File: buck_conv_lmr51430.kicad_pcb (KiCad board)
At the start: 2 copper layers, 43.2 x 17.4 mm, 10 parts, among them J1 Screw_Terminal_01x02, J2 Screw_Terminal_01x02

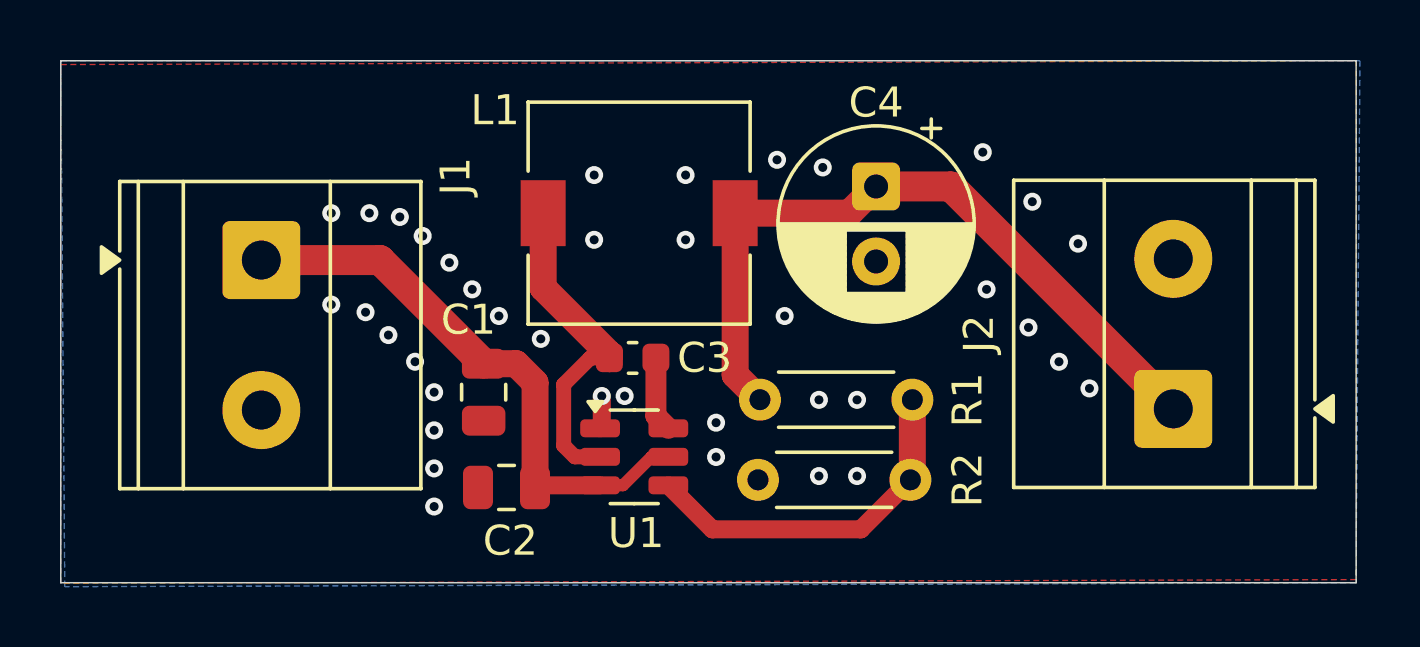
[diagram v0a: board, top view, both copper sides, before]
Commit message: Add variable output feedback network
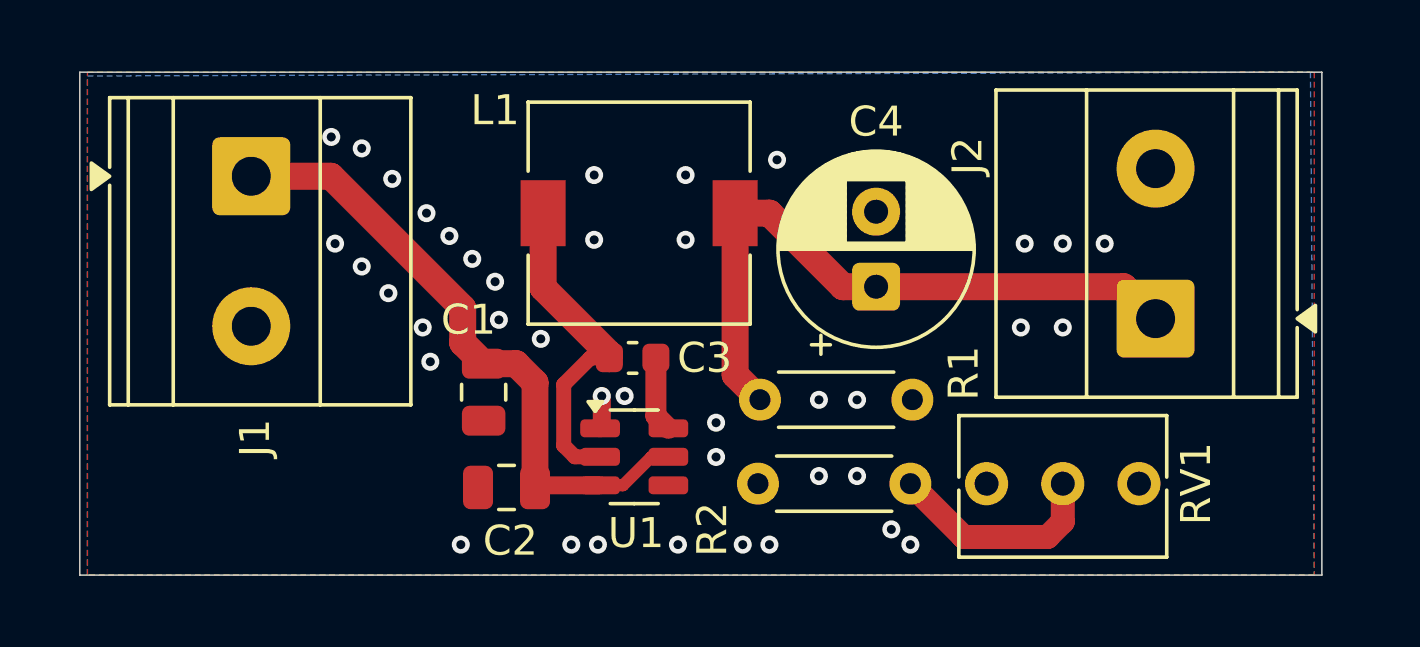
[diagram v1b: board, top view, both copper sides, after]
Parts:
- added RV1: 200k, Potentiometer_THT:Potentiometer_Bourns_3266Y_Vertical, F.Cu at (137.5, 96.6)
- moved R2 5.08 mm to (124.8, 96.6), turned to 0 degrees
- moved C4 3.34 mm to (128.8, 90.1), turned to 90 degrees
- moved J2 3.07 mm to (138.1, 91.1)
- moved J1 2.81 mm to (108.0, 86.4)
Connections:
- R1 pad 2: Net-(U1-FB) -> GND
- R2 pad 1: Net-(U1-FB) -> GND
- R2 pad 2: GND -> Net-(R2-Pad2)
- U1 pad 4: Net-(U1-FB) -> GND
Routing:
- net Net-(U1-FB): track 12.4 -> 0.00 mm
- net Net-(R2-Pad2): track 0.00 -> 7.39 mm
- net Net-(J2-Pin_1): track 24.6 -> 22.1 mm
- net Net-(J1-Pin_1): track 19.5 -> 21.7 mm
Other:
- board size 43.2 x 17.4 mm -> 41.4 x 16.8 mm

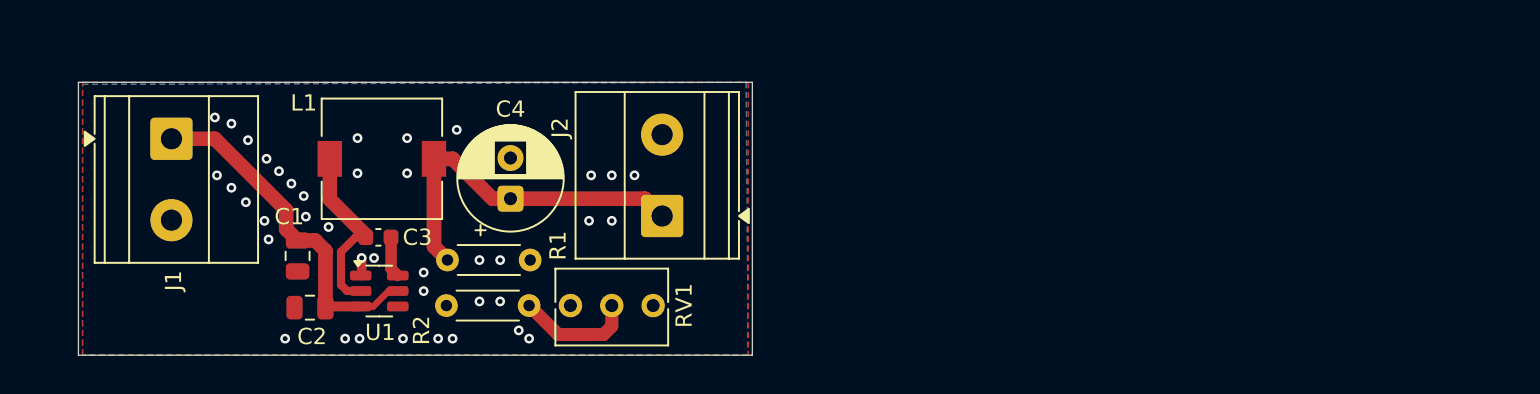
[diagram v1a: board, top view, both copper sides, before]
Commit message: Inductor selection and footprint fix
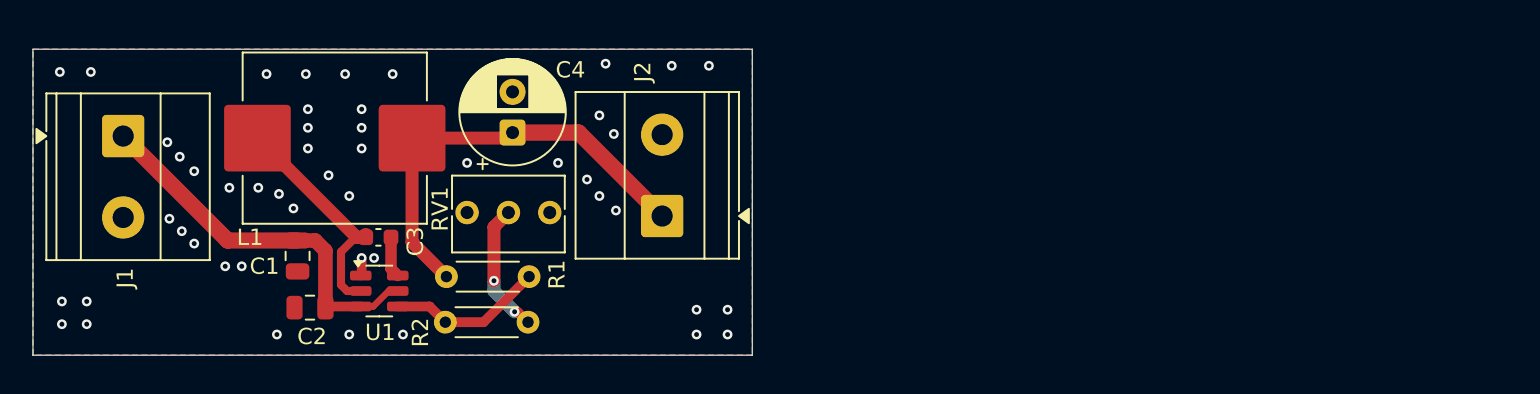
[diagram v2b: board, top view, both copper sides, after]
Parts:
- L1: footprint Inductor_SMD:L_7.3x7.3_H4.5 -> Inductor_SMD:L_APV_APH1030
- moved RV1 8.54 mm to (131.2, 90.9)
- moved C4 4.07 mm to (128.9, 86.0)
- moved L1 3.16 mm to (118.0, 86.4)
- moved J1 2.97 mm to (105.0, 86.2)
- moved R1 1.02 mm to (124.8, 94.9)
- moved R2 1.02 mm to (124.8, 97.7)
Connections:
- R1 pad 2: GND -> Net-(U1-FB)
- R2 pad 1: GND -> Net-(U1-FB)
- U1 pad 4: GND -> Net-(U1-FB)
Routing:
- net Net-(U1-FB): track 0.00 -> 9.98 mm
- net Net-(J2-Pin_1): track 22.1 -> 27.0 mm
- net Net-(U1-SW): track 11.4 -> 15.0 mm
- net Net-(J1-Pin_1): track 21.7 -> 24.0 mm
- net Net-(R2-Pad2): track 7.39 -> 8.08 mm, vias 0 -> 2
- net GND: track 1.45 -> 1.10 mm, vias 40 -> 49
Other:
- board size 41.4 x 16.8 mm -> 44.2 x 18.8 mm

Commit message: changes regarding the inductor
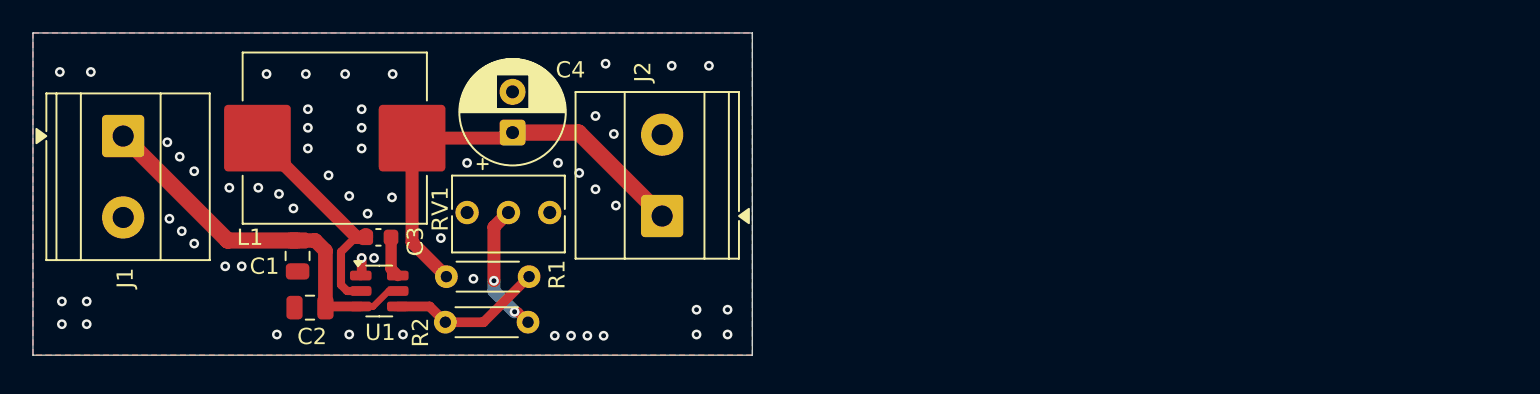
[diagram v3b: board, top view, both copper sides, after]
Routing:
- net GND: vias 49 -> 57
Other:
- board size 44.2 x 18.8 mm -> 44.2 x 19.8 mm
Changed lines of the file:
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@@
 			)
 		)
-		(property "Datasheet" ""
+		(property "Datasheet" "~"
 			(at 0 0 90)
 			(layer "F.Fab")
@@
 			)
 		)
-		(property "Datasheet" ""
+		(property "Datasheet" "~"
 			(at 0 0 90)
 			(layer "F.Fab")
@@
 			)
 		)
-		(property "Datasheet" ""
+		(property "Datasheet" "~"
 			(at 0 0 0)
 			(layer "F.Fab")
@@
 			)
 		)
-		(property "Datasheet" ""
+		(property "Datasheet" "~"
 			(at 0 0 0)
 			(layer "F.Fab")
@@
 			)
 		)
-		(property "Datasheet" ""
+		(property "Datasheet" "~"
 			(at 0 0 0)
 			(layer "F.Fab")
@@
 			)
 		)
-		(property "Datasheet" ""
+		(property "Datasheet" "~"
 			(at 0 0 90)
 			(layer "F.Fab")
@@
 			)
 		)
-		(property "Datasheet" ""
+		(property "Datasheet" "~"
 			(at 0 0 90)
 			(layer "F.Fab")
@@
 			)
 		)
-		(property "Datasheet" ""
+		(property "Datasheet" "~"
 			(at 0 0 0)
 			(layer "F.Fab")
@@
 			)
 		)
-		(property "Datasheet" ""
+		(property "Datasheet" "~"
 			(at 0 0 0)
 			(layer "F.Fab")
@@
 			)
 		)
-		(property "Datasheet" ""
+		(property "Datasheet" "~"
 			(at 0 0 0)
 			(layer "F.Fab")
@@
 	)
 	(gr_rect
-		(start 99.441 80.899)
+		(start 99.441 79.899)
 		(end 143.637 99.695)
 		(stroke
@@
 	)
 	(via
+		(at 120 91)
+		(size 0.6)
+		(drill 0.3)
+		(layers "F.Cu" "B.Cu")
+		(free yes)
+		(net 1)
+	)
+	(via
 		(at 112.268 94.234)
 		(size 0.6)
@@
 	)
 	(via
-		(at 134.239 84.963)
+		(at 134 85)
 		(size 0.6)
 		(drill 0.3)
@@
 	)
 	(via
+		(at 132.5 98.5)
+		(size 0.6)
+		(drill 0.3)
+		(layers "F.Cu" "B.Cu")
+		(free yes)
+		(net 1)
+	)
+	(via
 		(at 111.506 89.408)
 		(size 0.6)
@@
 	)
 	(via
-		(at 133.477 88.9)
+		(at 126.5 95)
+		(size 0.6)
+		(drill 0.3)
+		(layers "F.Cu" "B.Cu")
+		(free yes)
+		(net 1)
+	)
+	(via
+		(at 133 88.5)
 		(size 0.6)
 		(drill 0.3)
@@
 	)
 	(via
+		(at 134.5 98.5)
+		(size 0.6)
+		(drill 0.3)
+		(layers "F.Cu" "B.Cu")
+		(free yes)
+		(net 1)
+	)
+	(via
 		(at 113.284 89.408)
 		(size 0.6)
@@
 	)
 	(via
+		(at 133.5 98.5)
+		(size 0.6)
+		(drill 0.3)
+		(layers "F.Cu" "B.Cu")
+		(free yes)
+		(net 1)
+	)
+	(via
 		(at 116.205 82.423)
 		(size 0.6)
@@
 	)
 	(via
-		(at 135.255 90.805)
+		(at 135.255 90.5)
 		(size 0.6)
 		(drill 0.3)
@@
 	)
 	(via
-		(at 134.239 89.916)
+		(at 131.5 98.5)
+		(size 0.6)
+		(drill 0.3)
+		(layers "F.Cu" "B.Cu")
+		(free yes)
+		(net 1)
+	)
+	(via
+		(at 134 89.5)
 		(size 0.6)
 		(drill 0.3)
@@
 	)
 	(via
+		(at 124.5 92.5)
+		(size 0.6)
+		(drill 0.3)
+		(layers "F.Cu" "B.Cu")
+		(free yes)
+		(net 1)
+	)
+	(via
+		(at 121.5 90)
+		(size 0.6)
+		(drill 0.3)
+		(layers "F.Cu" "B.Cu")
+		(free yes)
+		(net 1)
+	)
+	(via
 		(at 116.332 86.995)
 		(size 0.6)
@@
 	)
 	(segment
-		(start 119.888 92.837)
-		(end 119.888 92.456)
-		(width 0.2)
-		(layer "F.Cu")
-		(net 3)
-	)
-	(segment
 		(start 118.364 95.377)
 		(end 118.364 93.345)
@@
 		(polygon
 			(pts
-				(xy 99.441 80.899) (xy 143.637 80.899) (xy 143.637 99.695) (xy 99.441 99.695)
+				(xy 99.441 79.899) (xy 143.637 79.899) (xy 143.637 99.695) (xy 99.441 99.695)
 			)
 		)
@@
 		(polygon
 			(pts
-				(xy 99.441 80.899) (xy 143.637 80.899) (xy 143.637 99.695) (xy 99.441 99.695)
+				(xy 99.441 79.899) (xy 143.637 79.899) (xy 143.637 99.695) (xy 99.441 99.695)
 			)
 		)

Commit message: rajath final touches
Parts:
- added C5: 22u, Capacitor_SMD:C_0805_2012Metric_Pad1.18x1.45mm_HandSolder, F.Cu at (169.0, 90.0)
- added C6: 22u, Capacitor_SMD:C_0805_2012Metric_Pad1.18x1.45mm_HandSolder, F.Cu at (175.0, 90.0)
- C1: value 1uF -> 4.7u; footprint Capacitor_SMD:C_0805_2012Metric -> Capacitor_SMD:C_0805_2012Metric_Pad1.18x1.45mm_HandSolder
- C2: value 100nF -> 100n; footprint Capacitor_SMD:C_0805_2012Metric -> Capacitor_SMD:C_0805_2012Metric_Pad1.18x1.45mm_HandSolder
- C3: value 100nF -> 100n; footprint Capacitor_SMD:C_0603_1608Metric -> Capacitor_SMD:C_0805_2012Metric_Pad1.18x1.45mm_HandSolder
- C4: value 100uF -> 22u; footprint Capacitor_THT:CP_Radial_D6.3mm_P2.50mm -> Capacitor_SMD:C_0805_2012Metric_Pad1.18x1.45mm_HandSolder
- J1: value Screw_Terminal_01x02 -> Input
- J2: value Screw_Terminal_01x02 -> Output
- L1: value 5.6uH -> 12u
- R1: value 100k -> 100K; footprint Resistor_THT:R_Axial_DIN0204_L3.6mm_D1.6mm_P5.08mm_Horizontal -> Resistor_SMD:R_0805_2012Metric_Pad1.20x1.40mm_HandSolder
- R2: value 22.1 -> 5K; footprint Resistor_THT:R_Axial_DIN0204_L3.6mm_D1.6mm_P5.08mm_Horizontal -> Resistor_SMD:R_0805_2012Metric_Pad1.20x1.40mm_HandSolder
- RV1: value 200k -> 20K
- U1: value ~ -> LMR51430
- moved J2 46.1 mm to (184.2, 92.5)
- moved RV1 43.6 mm to (174.5, 95.5)
- moved C4 43.3 mm to (172.0, 90.0), turned to -90 degrees
- moved R1 41.4 mm to (166.0, 90.0), turned to -90 degrees
- moved R2 41.3 mm to (166.0, 95.0), turned to -90 degrees
- moved C1 39.9 mm to (155.5, 97.0), turned to 0 degrees
- moved C3 39.8 mm to (160.0, 86.5), turned to 90 degrees
- moved C2 39.1 mm to (155.5, 94.0), turned to 0 degrees
- moved U1 35.3 mm to (155.5, 90.0)
- moved L1 23.0 mm to (141.0, 87.0), turned to 180 degrees
- moved J1 20.9 mm to (125.8, 87.5)
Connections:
- net Net-(J1-Pin_1) renamed /VIN
- net Net-(U1-FB) renamed /FB
- net Net-(U1-SW) renamed /SW
- C4 pad 1: Net-(J2-Pin_1) -> /VOUT
- J2 pad 1: Net-(J2-Pin_1) -> GND
- J2 pad 2: GND -> /VOUT
- L1 pad 2: Net-(J2-Pin_1) -> /VOUT
- R1 pad 1: Net-(J2-Pin_1) -> /VOUT
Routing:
- net /VOUT: track 0.00 -> 53.8 mm
- net Net-(J2-Pin_1): track 27.0 -> 0.00 mm
- net /VIN: track 24.0 -> 37.6 mm, vias 0 -> 7
- net /SW: track 14.6 -> 11.6 mm, vias 0 -> 7
- net /FB: track 9.98 -> 12.4 mm
- net Net-(U1-CB): track 2.52 -> 3.99 mm
- net GND: track 1.10 -> 0.00 mm, vias 57 -> 94
- net Net-(R2-Pad2): track 8.08 -> 7.45 mm, vias 2 -> 0
- added copper zone on F.Cu, net /SW
- added copper zone on B.Cu, net /VIN
- added copper zone on F.Cu, net /VIN
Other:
- board size 44.2 x 19.8 mm -> 70 x 20 mm
